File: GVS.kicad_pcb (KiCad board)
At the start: 2 copper layers, 78 x 53 mm, 28 parts, among them J1 Conn_01x19_Socket, J10 Conn_01x02_Pin, J11 Conn_01x02_Pin, J2 Conn_01x02_Pin, J3 Conn_01x19_Socket, J4 Conn_01x02_Pin, J5 Conn_01x02_Pin, J6 Conn_01x19_Pin, J7 Conn_01x19_Pin, J8 Conn_01x02_Pin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

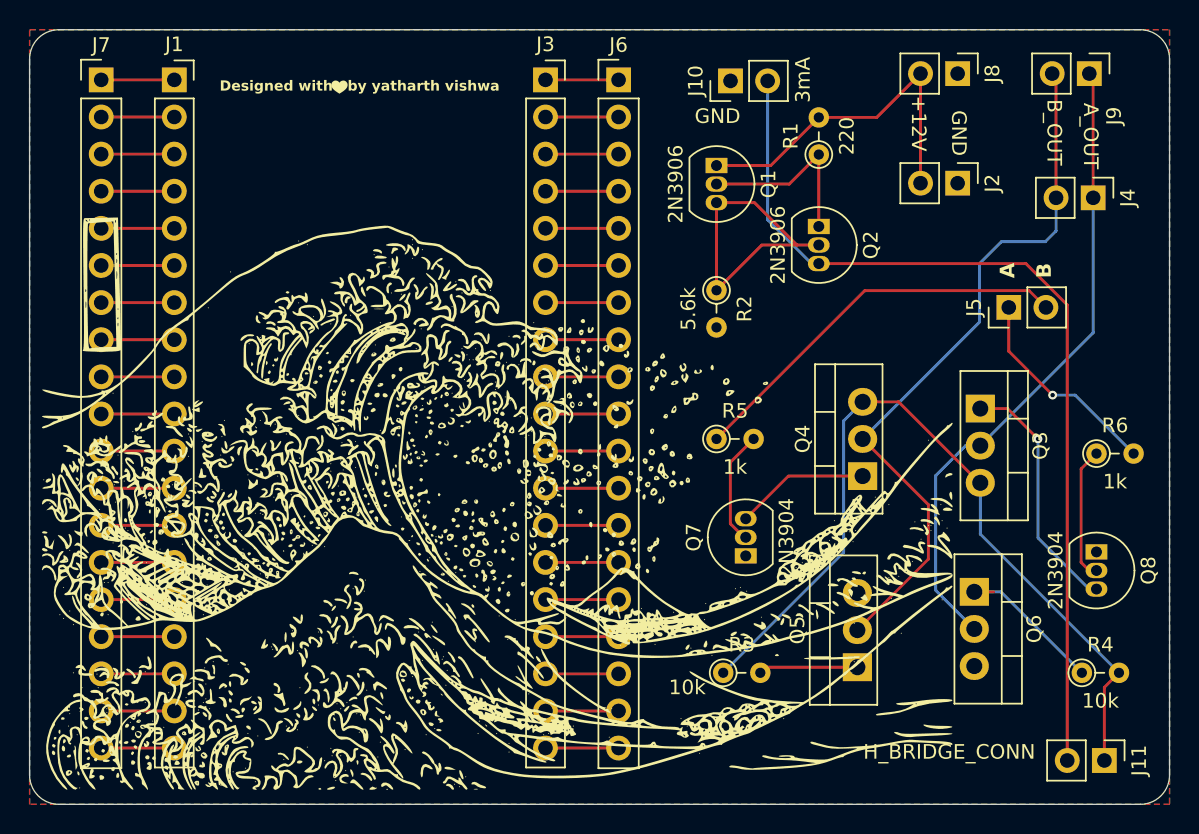
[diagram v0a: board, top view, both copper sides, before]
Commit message: added screw terminals
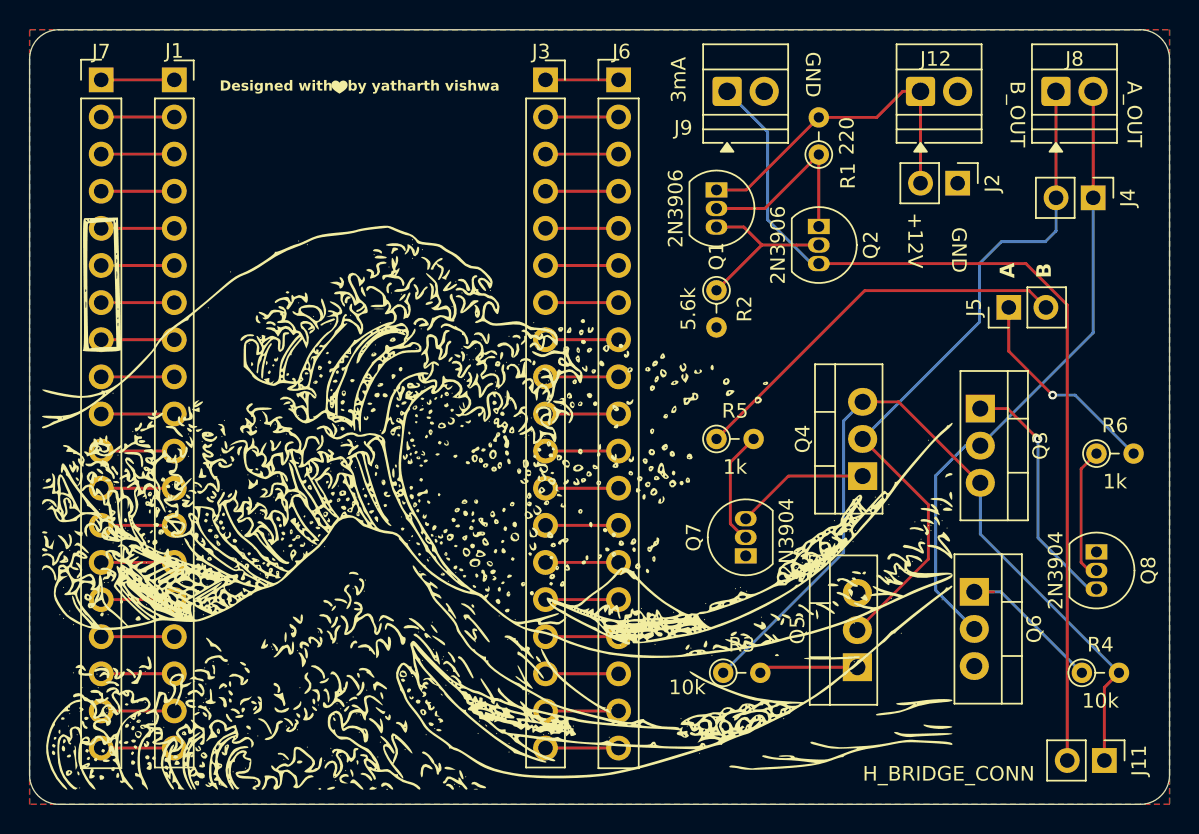
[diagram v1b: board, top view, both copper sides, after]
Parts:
- removed J10: Conn_01x02_Pin, Connector_PinHeader_2.54mm:PinHeader_1x02_P2.54mm_Vertical
- added J12: Screw_Terminal_01x02, TerminalBlock:TerminalBlock_Xinya_XY308-2.54-2P_1x02_P2.54mm_Horizontal, F.Cu at (134.0, 63.2)
- J8, J9: value Conn_01x02_Pin -> Screw_Terminal_01x02; footprint Connector_PinHeader_2.54mm:PinHeader_1x02_P2.54mm_Vertical -> TerminalBlock:TerminalBlock_Xinya_XY308-2.54-2P_1x02_P2.54mm_Horizontal
- moved J9 24.8 mm to (120.7, 63.2), turned to 0 degrees
- moved J8 6.83 mm to (143.2, 63.2), turned to 0 degrees
- moved Q1 1.67 mm to (120.0, 70.0)
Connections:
- J8 pad 1: GND -> A_OUT
- J8 pad 2: +12V -> B_OUT
- J9 pad 1: B_OUT -> 3mA limit
- J9 pad 2: A_OUT -> GND
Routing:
- net Net-(Q1-C): track 21.0 -> 11.9 mm
- net B_OUT: track 44.3 -> 42.9 mm
- net A_OUT: track 49.3 -> 48.0 mm
- net +12V: track 24.1 -> 23.0 mm
- net Net-(Q1-B): track 12.8 -> 13.4 mm
